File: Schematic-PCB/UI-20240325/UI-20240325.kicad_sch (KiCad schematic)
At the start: 18 parts, among them J1 Conn_01x10_Pin, SW1 SW_Push, SW2 SW_Push, SW3 SW_Push, SW4 SW_Push, SW5 SW_Push

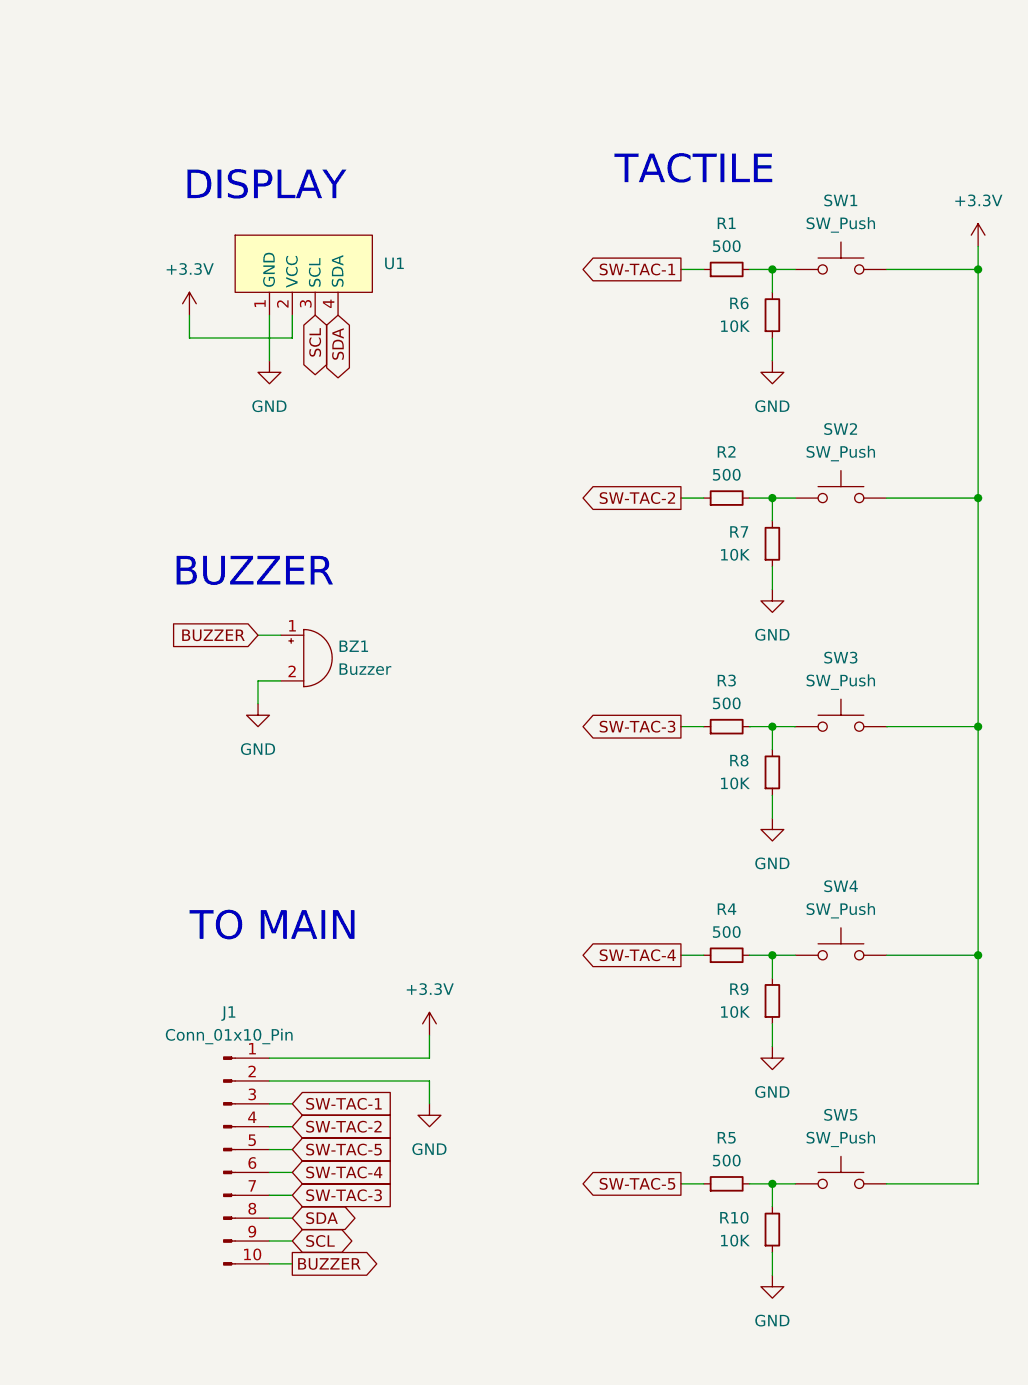
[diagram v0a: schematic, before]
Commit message: update: UI基板の更新など
発注用ファイルの出力・UI基板の仕様変更
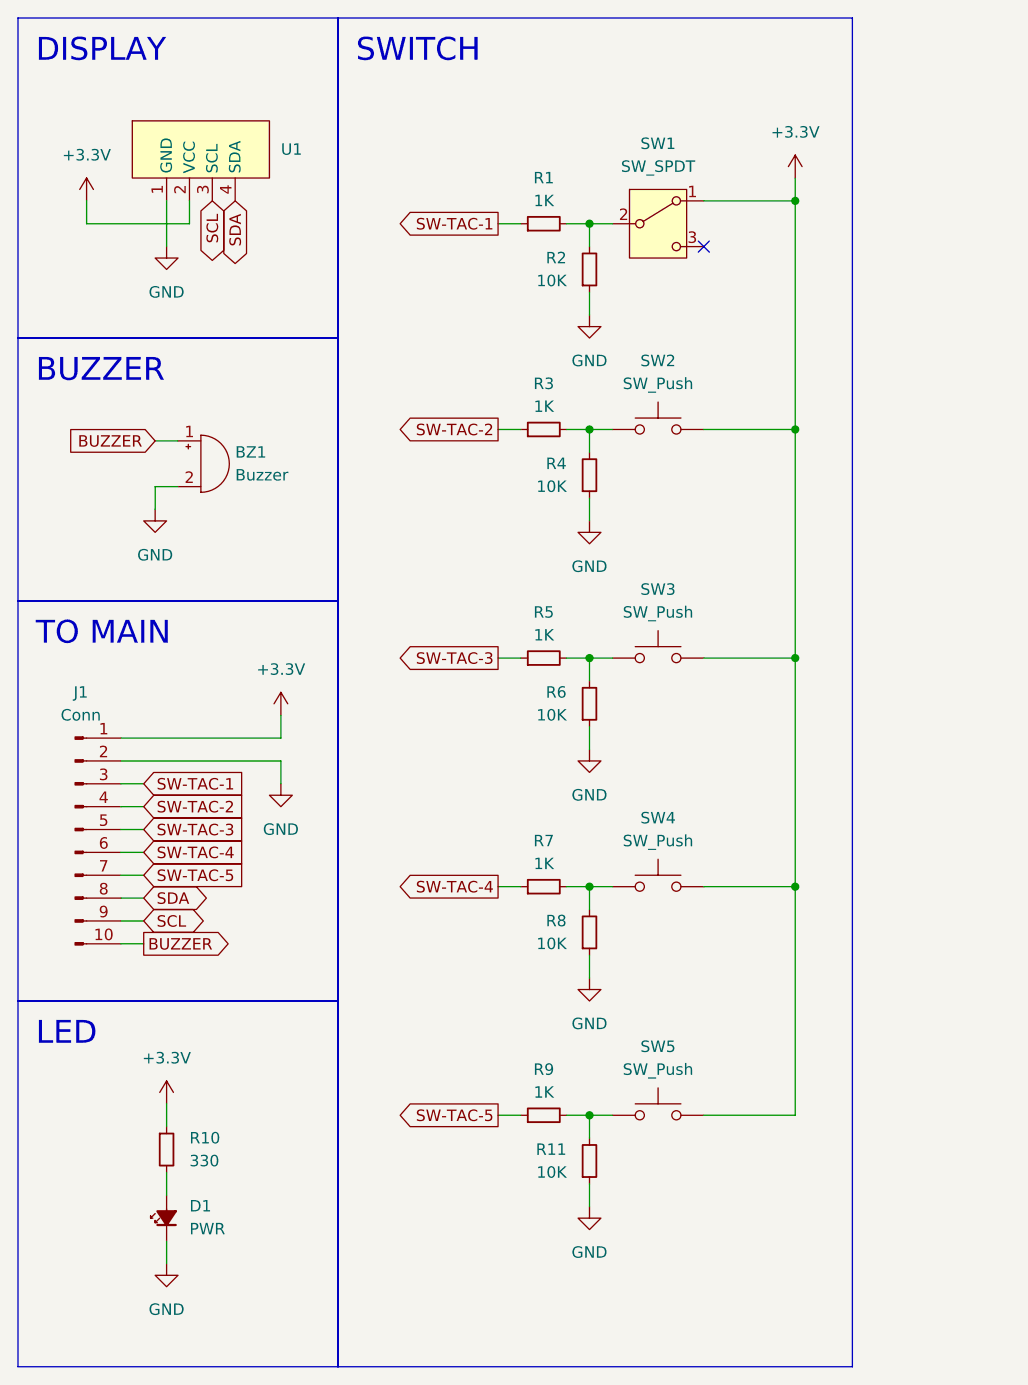
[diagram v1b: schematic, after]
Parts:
- removed R2, R4: 500, Resistor_SMD:R_0603_1608Metric, symbol Device:R_Small
- removed SW1: SW_Push, @2024TOINIOT2-UI:TVBP06-B043C, symbol Switch:SW_Push
- added D1: PWR, LED_SMD:LED_0603_1608Metric, symbol Device:LED_Small_Filled
- added R11: 10K, Resistor_SMD:R_0603_1608Metric, symbol Device:R_Small
- added R7, R9: 1K, Resistor_SMD:R_0603_1608Metric, symbol Device:R_Small
- added SW1: SW_SPDT, @2024TOINIOT2-UI:2MS1-T1-B4-VS2-Q-E-S, symbol Switch:SW_SPDT
- J1: value Conn_01x10_Pin -> Conn
- R1, R3, R5: value 500 -> 1K
- R10: value 10K -> 330
- renumbered R6 to R2, R7 to R4, R8 to R6, R9 to R8
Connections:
- net +3.3V: now also R10.1, SW1.1 (A)
- net GND: now also D1.1 (K), R11.1; no longer R10.1
- net SW-TAC-2: now also R3.1
- net SW-TAC-3: now also J1.5 (Pin_5), R5.1; no longer J1.7 (Pin_7), R3.1
- net SW-TAC-4: now also R7.1
- net SW-TAC-5: now also J1.7 (Pin_7), R9.1; no longer J1.5 (Pin_5), R5.1
- net at R1.2, R2.2: now also SW1.2 (B)
- net at R6.2, SW3.1: now also R5.2; no longer R3.2
- net at R4.2, SW2.1: now also R3.2
- net at R8.2, SW4.1: now also R7.2
- new net: D1.2 (A), R10.2
- new net: R11.2, R9.2, SW5.1
- no-connect marks 0 -> 1
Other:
- note removed: "BUZZER"
- note removed: "DISPLAY"
- note removed: "TACTILE"
- note removed: "TO MAIN"
- moved on the sheet: BZ1, J1, R1, R2, R4, R6, R8, SW2, SW3, SW4, U1

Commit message: update: UI基板のグローバルラベル名が間違っていたのを修正した
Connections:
- net SW-TAC-5 is gone; now on net SW-TAC-4: J1.7 (Pin_7), R9.1
- net SW-TAC-1: now also J1.4 (Pin_4), R3.1; no longer J1.3 (Pin_3), R1.1
- net SW-TAC-2: now also J1.5 (Pin_5), R5.1; no longer J1.4 (Pin_4), R3.1
- net SW-TAC-3: now also J1.6 (Pin_6), R7.1; no longer J1.5 (Pin_5), R5.1
- net SW-TAC-4: no longer J1.6 (Pin_6), R7.1
- new net SW-TOG: J1.3 (Pin_3), R1.1
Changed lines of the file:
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@@
 		)
 	)
-	(global_label "SW-TAC-2"
+	(global_label "SW-TAC-1"
 		(shape input)
 		(at 26.67 100.33 0)
@@
 		)
 	)
+	(global_label "SW-TOG"
+		(shape input)
+		(at 26.67 97.79 0)
+		(fields_autoplaced yes)
+		(effects
+			(font
+				(size 1.27 1.27)
+			)
+			(justify left)
+		)
+		(property "Intersheetrefs" "${INTERSHEET_REFS}"
+			(at 38.7396 97.79 0)
+			(effects
+				(font
+					(size 1.27 1.27)
+				)
+				(justify left)
+				(hide yes)
+			)
+		)
+	)
 	(global_label "SW-TAC-1"
-		(shape input)
-		(at 26.67 97.79 0)
-		(fields_autoplaced yes)
-		(effects
-			(font
-				(size 1.27 1.27)
-			)
-			(justify left)
-		)
-		(property "Intersheetrefs" "${INTERSHEET_REFS}"
-			(at 38.7396 97.79 0)
-			(effects
-				(font
-					(size 1.27 1.27)
-				)
-				(justify left)
+		(shape output)
+		(at 66.04 58.42 180)
+		(fields_autoplaced yes)
+		(effects
+			(font
+				(size 1.27 1.27)
+			)
+			(justify right)
+		)
+		(property "Intersheetrefs" "${INTERSHEET_REFS}"
+			(at 53.9704 58.42 0)
+			(effects
+				(font
+					(size 1.27 1.27)
+				)
+				(justify right)
 				(hide yes)
 			)
@@
 	)
 	(global_label "SW-TAC-2"
-		(shape output)
-		(at 66.04 58.42 180)
-		(fields_autoplaced yes)
-		(effects
-			(font
-				(size 1.27 1.27)
-			)
-			(justify right)
-		)
-		(property "Intersheetrefs" "${INTERSHEET_REFS}"
-			(at 53.9704 58.42 0)
-			(effects
-				(font
-					(size 1.27 1.27)
-				)
-				(justify right)
-				(hide yes)
-			)
-		)
-	)
-	(global_label "SW-TAC-3"
 		(shape output)
 		(at 66.04 83.82 180)
@@
 		)
 	)
+	(global_label "SW-TAC-3"
+		(shape output)
+		(at 66.04 109.22 180)
+		(fields_autoplaced yes)
+		(effects
+			(font
+				(size 1.27 1.27)
+			)
+			(justify right)
+		)
+		(property "Intersheetrefs" "${INTERSHEET_REFS}"
+			(at 53.9704 109.22 0)
+			(effects
+				(font
+					(size 1.27 1.27)
+				)
+				(justify right)
+				(hide yes)
+			)
+		)
+	)
 	(global_label "SW-TAC-4"
 		(shape output)
-		(at 66.04 109.22 180)
-		(fields_autoplaced yes)
-		(effects
-			(font
-				(size 1.27 1.27)
-			)
-			(justify right)
-		)
-		(property "Intersheetrefs" "${INTERSHEET_REFS}"
-			(at 53.9704 109.22 0)
-			(effects
-				(font
-					(size 1.27 1.27)
-				)
-				(justify right)
-				(hide yes)
-			)
-		)
-	)
-	(global_label "SW-TAC-5"
-		(shape output)
 		(at 66.04 134.62 180)
 		(fields_autoplaced yes)
@@
 		)
 	)
+	(global_label "SW-TAC-3"
+		(shape input)
+		(at 26.67 105.41 0)
+		(fields_autoplaced yes)
+		(effects
+			(font
+				(size 1.27 1.27)
+			)
+			(justify left)
+		)
+		(property "Intersheetrefs" "${INTERSHEET_REFS}"
+			(at 38.7396 105.41 0)
+			(effects
+				(font
+					(size 1.27 1.27)
+				)
+				(justify left)
+				(hide yes)
+			)
+		)
+	)
+	(global_label "SW-TOG"
+		(shape output)
+		(at 66.04 35.56 180)
+		(fields_autoplaced yes)
+		(effects
+			(font
+				(size 1.27 1.27)
+			)
+			(justify right)
+		)
+		(property "Intersheetrefs" "${INTERSHEET_REFS}"
+			(at 53.9704 35.56 0)
+			(effects
+				(font
+					(size 1.27 1.27)
+				)
+				(justify right)
+				(hide yes)
+			)
+		)
+	)
+	(global_label "SW-TAC-2"
+		(shape input)
+		(at 26.67 102.87 0)
+		(fields_autoplaced yes)
+		(effects
+			(font
+				(size 1.27 1.27)
+			)
+			(justify left)
+		)
+		(property "Intersheetrefs" "${INTERSHEET_REFS}"
+			(at 38.7396 102.87 0)
+			(effects
+				(font
+					(size 1.27 1.27)
+				)
+				(justify left)
+				(hide yes)
+			)
+		)
+	)
+	(global_label "BUZZER"
+		(shape input)
+		(at 27.94 59.69 180)
+		(fields_autoplaced yes)
+		(effects
+			(font
+				(size 1.27 1.27)
+			)
+			(justify right)
+		)
+		(property "Intersheetrefs" "${INTERSHEET_REFS}"
+			(at 17.1297 59.69 0)
+			(effects
+				(font
+					(size 1.27 1.27)
+				)
+				(justify right)
+				(hide yes)
+			)
+		)
+	)
+	(global_label "BUZZER"
+		(shape output)
+		(at 26.67 115.57 0)
+		(fields_autoplaced yes)
+		(effects
+			(font
+				(size 1.27 1.27)
+			)
+			(justify left)
+		)
+		(property "Intersheetrefs" "${INTERSHEET_REFS}"
+			(at 37.4803 115.57 0)
+			(effects
+				(font
+					(size 1.27 1.27)
+				)
+				(justify left)
+				(hide yes)
+			)
+		)
+	)
 	(global_label "SW-TAC-4"
 		(shape input)
-		(at 26.67 105.41 0)
-		(fields_autoplaced yes)
-		(effects
-			(font
-				(size 1.27 1.27)
-			)
-			(justify left)
-		)
-		(property "Intersheetrefs" "${INTERSHEET_REFS}"
-			(at 38.7396 105.41 0)
-			(effects
-				(font
-					(size 1.27 1.27)
-				)
-				(justify left)
-				(hide yes)
-			)
-		)
-	)
-	(global_label "SW-TAC-1"
-		(shape output)
-		(at 66.04 35.56 180)
-		(fields_autoplaced yes)
-		(effects
-			(font
-				(size 1.27 1.27)
-			)
-			(justify right)
-		)
-		(property "Intersheetrefs" "${INTERSHEET_REFS}"
-			(at 53.9704 35.56 0)
-			(effects
-				(font
-					(size 1.27 1.27)
-				)
-				(justify right)
-				(hide yes)
-			)
-		)
-	)
-	(global_label "SW-TAC-3"
-		(shape input)
-		(at 26.67 102.87 0)
-		(fields_autoplaced yes)
-		(effects
-			(font
-				(size 1.27 1.27)
-			)
-			(justify left)
-		)
-		(property "Intersheetrefs" "${INTERSHEET_REFS}"
-			(at 38.7396 102.87 0)
-			(effects
-				(font
-					(size 1.27 1.27)
-				)
-				(justify left)
-				(hide yes)
-			)
-		)
-	)
-	(global_label "BUZZER"
-		(shape input)
-		(at 27.94 59.69 180)
-		(fields_autoplaced yes)
-		(effects
-			(font
-				(size 1.27 1.27)
-			)
-			(justify right)
-		)
-		(property "Intersheetrefs" "${INTERSHEET_REFS}"
-			(at 17.1297 59.69 0)
-			(effects
-				(font
-					(size 1.27 1.27)
-				)
-				(justify right)
-				(hide yes)
-			)
-		)
-	)
-	(global_label "BUZZER"
-		(shape output)
-		(at 26.67 115.57 0)
-		(fields_autoplaced yes)
-		(effects
-			(font
-				(size 1.27 1.27)
-			)
-			(justify left)
-		)
-		(property "Intersheetrefs" "${INTERSHEET_REFS}"
-			(at 37.4803 115.57 0)
-			(effects
-				(font
-					(size 1.27 1.27)
-				)
-				(justify left)
-				(hide yes)
-			)
-		)
-	)
-	(global_label "SW-TAC-5"
-		(shape input)
 		(at 26.67 107.95 0)

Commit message: UI基板の各ボタンにチャタリング防止用コンデンサを配置した
ただしトグルスイッチを除く()
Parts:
- added C1, C2, C3, C4: 0.1uF, Capacitor_SMD:C_0603_1608Metric, symbol Device:C_Small
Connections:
- net +3.3V: now also C1.2, C2.2, C3.2, C4.2
- net at R7.2, R8.2, SW4.1: now also C3.1
- net at R3.2, R4.2, SW2.1: now also C1.1
- net at R5.2, R6.2, SW3.1: now also C2.1
- net at R11.2, R9.2, SW5.1: now also C4.1
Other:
- moved on the sheet: SW1, SW2, SW3, SW4, SW5
